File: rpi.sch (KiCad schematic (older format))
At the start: 14 parts, among them J1 40HAT, Q1 DMMT5401, Q2 DMG2305UX, U1 CAT24C32

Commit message: Current snapshot
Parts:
- added H5, H6, H7: 3mm_Mounting_Hole, MountingHole:MountingHole_3mm, symbol Mechanical:MountingHole
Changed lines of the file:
@@
 $Descr A4 11693 8268
 encoding utf-8
-Sheet 2 7
+Sheet 2 11
 Title "Raspberry Pi Connector"
 Date ""
@@
 $EndComp
 NoConn ~ 2650 1900
+$Comp
+L Mechanical:MountingHole H5
+U 1 1 5BC57D78
+P 9050 4600
+F 0 "H5" H 8900 4700 60  0000 C CNN
+F 1 "3mm_Mounting_Hole" H 9050 4450 60  0000 C CNN
+F 2 "MountingHole:MountingHole_3mm" H 8950 4600 60  0001 C CNN
+F 3 "" H 8950 4600 60  0001 C CNN
+	1    9050 4600
+	1    0    0    -1
+$EndComp
+$Comp
+L Mechanical:MountingHole H7
+U 1 1 5BC57D7F
+P 10000 4600
+F 0 "H7" H 9850 4700 60  0000 C CNN
+F 1 "3mm_Mounting_Hole" H 10000 4450 60  0000 C CNN
+F 2 "MountingHole:MountingHole_3mm" H 9900 4600 60  0001 C CNN
+F 3 "" H 9900 4600 60  0001 C CNN
+	1    10000 4600
+	1    0    0    -1
+$EndComp
+$Comp
+L Mechanical:MountingHole H6
+U 1 1 5BC57D86
+P 9050 5100
+F 0 "H6" H 8900 5200 60  0000 C CNN
+F 1 "3mm_Mounting_Hole" H 9050 4950 60  0000 C CNN
+F 2 "MountingHole:MountingHole_3mm" H 8950 5100 60  0001 C CNN
+F 3 "" H 8950 5100 60  0001 C CNN
+	1    9050 5100
+	1    0    0    -1
+$EndComp
 $EndSCHEMATC

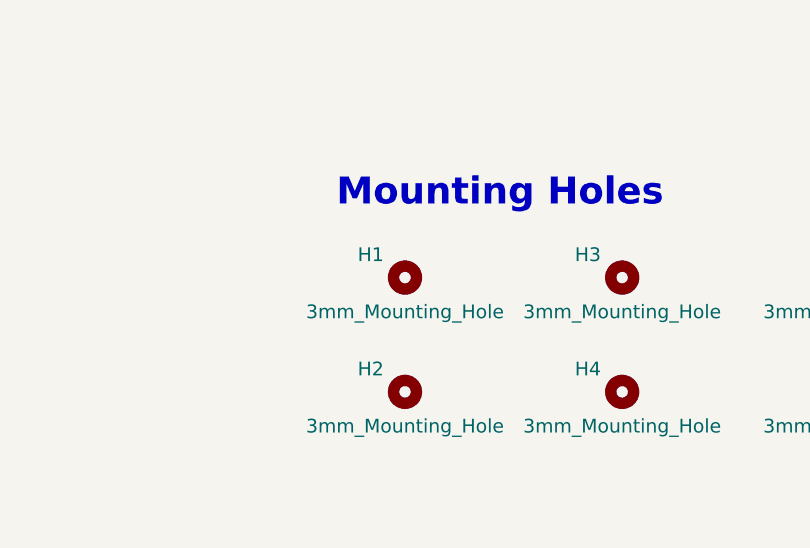
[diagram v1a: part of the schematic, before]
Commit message: Finished general layout and power planes
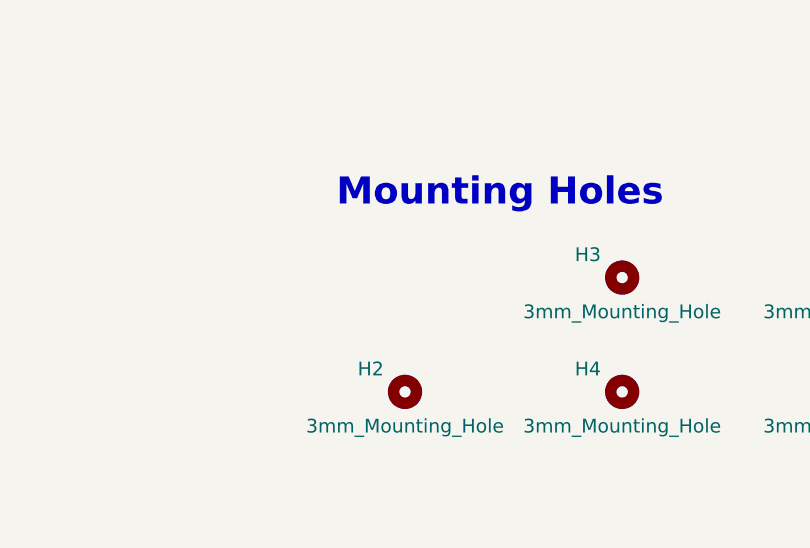
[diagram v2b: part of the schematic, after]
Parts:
- removed H1: 3mm_Mounting_Hole, MountingHole:MountingHole_3mm, symbol Mechanical:MountingHole
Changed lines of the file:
@@
 $EndDescr
-$Comp
-L Mechanical:MountingHole H1
-U 1 1 5BC4B184
-P 7050 4600
-F 0 "H1" H 6900 4700 60  0000 C CNN
-F 1 "3mm_Mounting_Hole" H 7050 4450 60  0000 C CNN
-F 2 "MountingHole:MountingHole_3mm" H 6950 4600 60  0001 C CNN
-F 3 "" H 6950 4600 60  0001 C CNN
-	1    7050 4600
-	1    0    0    -1
-$EndComp
 $Comp
 L heteromycin:OX40HAT J1

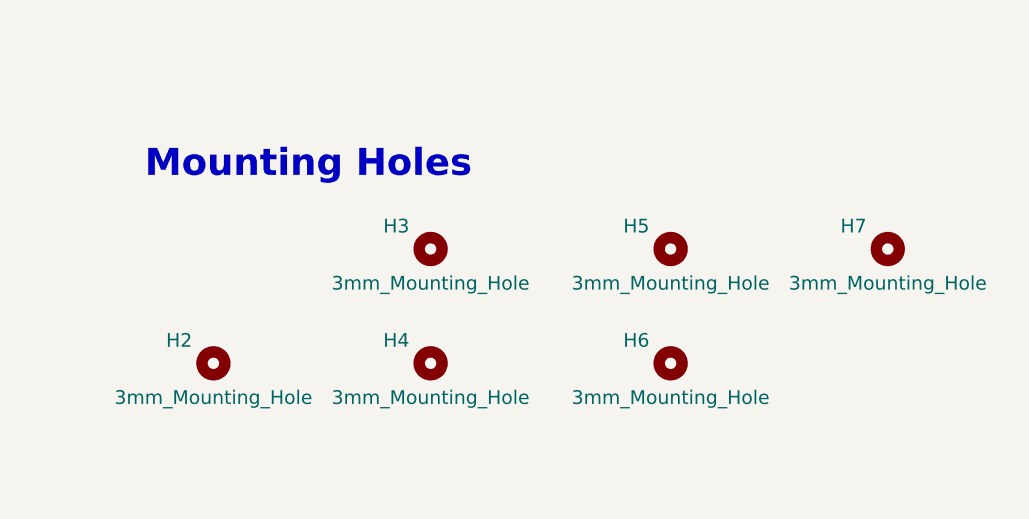
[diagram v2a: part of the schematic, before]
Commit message: Add SD card reader, placed temp connections, fixed stepper placement
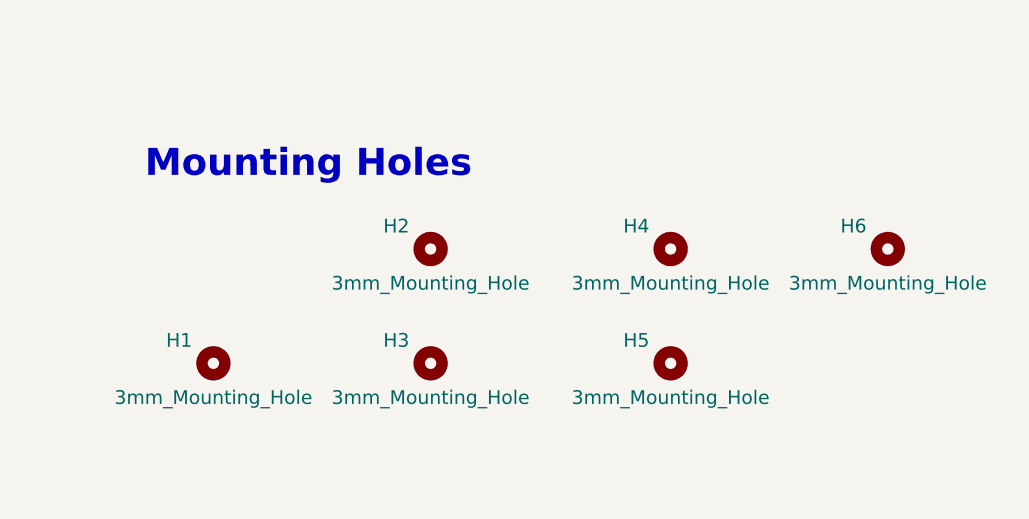
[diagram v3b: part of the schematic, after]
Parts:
- renumbered H2 to H1, H3 to H2, H4 to H3, H5 to H4, H6 to H5, H7 to H6
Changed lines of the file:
@@
 $Descr A4 11693 8268
 encoding utf-8
-Sheet 2 11
+Sheet 2 12
 Title "Raspberry Pi Connector"
 Date ""
@@
 $EndComp
 $Comp
-L Mechanical:MountingHole H3
+L Mechanical:MountingHole H2
 U 1 1 5BC4B22D
 P 8000 4600
-F 0 "H3" H 7850 4700 60  0000 C CNN
+F 0 "H2" H 7850 4700 60  0000 C CNN
 F 1 "3mm_Mounting_Hole" H 8000 4450 60  0000 C CNN
 F 2 "MountingHole:MountingHole_3mm" H 7900 4600 60  0001 C CNN
@@
 $EndComp
 $Comp
-L Mechanical:MountingHole H2
+L Mechanical:MountingHole H1
 U 1 1 5BC4B234
 P 7050 5100
-F 0 "H2" H 6900 5200 60  0000 C CNN
+F 0 "H1" H 6900 5200 60  0000 C CNN
 F 1 "3mm_Mounting_Hole" H 7050 4950 60  0000 C CNN
 F 2 "MountingHole:MountingHole_3mm" H 6950 5100 60  0001 C CNN
@@
 $EndComp
 $Comp
-L Mechanical:MountingHole H4
+L Mechanical:MountingHole H3
 U 1 1 5BC4B23B
 P 8000 5100
-F 0 "H4" H 7850 5200 60  0000 C CNN
+F 0 "H3" H 7850 5200 60  0000 C CNN
 F 1 "3mm_Mounting_Hole" H 8000 4950 60  0000 C CNN
 F 2 "MountingHole:MountingHole_3mm" H 7900 5100 60  0001 C CNN
@@
 NoConn ~ 2650 1900
 $Comp
-L Mechanical:MountingHole H5
+L Mechanical:MountingHole H4
 U 1 1 5BC57D78
 P 9050 4600
-F 0 "H5" H 8900 4700 60  0000 C CNN
+F 0 "H4" H 8900 4700 60  0000 C CNN
 F 1 "3mm_Mounting_Hole" H 9050 4450 60  0000 C CNN
 F 2 "MountingHole:MountingHole_3mm" H 8950 4600 60  0001 C CNN
@@
 $EndComp
 $Comp
-L Mechanical:MountingHole H7
+L Mechanical:MountingHole H6
 U 1 1 5BC57D7F
 P 10000 4600
-F 0 "H7" H 9850 4700 60  0000 C CNN
+F 0 "H6" H 9850 4700 60  0000 C CNN
 F 1 "3mm_Mounting_Hole" H 10000 4450 60  0000 C CNN
 F 2 "MountingHole:MountingHole_3mm" H 9900 4600 60  0001 C CNN
@@
 $EndComp
 $Comp
-L Mechanical:MountingHole H6
+L Mechanical:MountingHole H5
 U 1 1 5BC57D86
 P 9050 5100
-F 0 "H6" H 8900 5200 60  0000 C CNN
+F 0 "H5" H 8900 5200 60  0000 C CNN
 F 1 "3mm_Mounting_Hole" H 9050 4950 60  0000 C CNN
 F 2 "MountingHole:MountingHole_3mm" H 8950 5100 60  0001 C CNN

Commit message: Some small adjustments
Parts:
- J1: value 40HAT -> 920-0135-01
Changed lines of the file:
@@
 P 3250 1100
 F 0 "J1" H 3600 1200 50  0000 C CNN
-F 1 "40HAT" H 2950 1200 50  0000 C CNN
+F 1 "920-0135-01" H 2950 1200 50  0000 C CNN
 F 2 "Connector_PinSocket_2.54mm:PinSocket_2x20_P2.54mm_Vertical" H 3250 1300 50  0001 C CNN
 F 3 "" H 2550 1100 50  0000 C CNN

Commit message: First pass of routing
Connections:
- net RX: now reaches J1.10 (BCM15)
- net nRESET: now reaches J1.12 (BCM18)
- net MOSI: now reaches J1.19 (BCM10)
- net MISO: now reaches J1.21 (BCM9)
- net SCLK: now reaches J1.23 (BCM11)
- net SS_0: now reaches J1.24 (BCM8)
- net SS_1: now reaches J1.26 (BCM7)
- net D1: now reaches J1.29 (BCM5)
- net SDA: now reaches J1.3 (BCM2)
- net D2: now reaches J1.31 (BCM6)
- net D3: now reaches J1.33 (BCM13)
- net D4: now reaches J1.35 (BCM19)
- net SCL: now reaches J1.5 (BCM3)
- net BOOT: now reaches J1.7 (BCM4)
- net TX: now reaches J1.8 (BCM14)
- no-connect marks 2 -> 13
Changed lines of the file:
@@
 	1    0    0    -1
 $EndComp
+Text HLabel 2650 1200 0    50   Input ~ 0
+SDA
+Text HLabel 2650 1300 0    50   Input ~ 0
+SCL
+Text HLabel 2650 1400 0    50   Input ~ 0
+BOOT
+Text HLabel 3850 1600 2    50   Input ~ 0
+nRESET
+Text HLabel 3850 1400 2    50   Input ~ 0
+TX
+Text HLabel 3850 1500 2    50   Input ~ 0
+RX
+Text HLabel 2650 2000 0    50   Input ~ 0
+MOSI
+Text HLabel 2650 2100 0    50   Input ~ 0
+MISO
+Text HLabel 2650 2200 0    50   Input ~ 0
+SCLK
+Text HLabel 3850 2200 2    50   Input ~ 0
+SS_0
+Text HLabel 3850 2300 2    50   Input ~ 0
+SS_1
+Text HLabel 2650 2500 0    50   Input ~ 0
+D1
+Text HLabel 2650 2600 0    50   Input ~ 0
+D2
+Text HLabel 2650 2700 0    50   Input ~ 0
+D3
+Text HLabel 2650 2800 0    50   Input ~ 0
+D4
+NoConn ~ 2650 1600
+NoConn ~ 2650 1700
+NoConn ~ 2650 1800
+NoConn ~ 2650 2900
+NoConn ~ 3850 1800
+NoConn ~ 3850 1900
+NoConn ~ 3850 2100
+NoConn ~ 3850 2600
+NoConn ~ 3850 2800
+NoConn ~ 3850 2900
+NoConn ~ 3850 3000
 $EndSCHEMATC

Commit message: Complete functional design
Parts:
- H1: renamed from H2; footprint MountingHole:MountingHole_3mm -> heteromycin:MountingHole_3mm
- H2: renamed from H1; footprint MountingHole:MountingHole_3mm -> heteromycin:MountingHole_3mm
- H3: renamed from H4; footprint MountingHole:MountingHole_3mm -> heteromycin:MountingHole_3mm
- H4: renamed from H3; footprint MountingHole:MountingHole_3mm -> heteromycin:MountingHole_3mm
- H5: renamed from H6; footprint MountingHole:MountingHole_3mm -> heteromycin:MountingHole_3mm
- H6: renamed from H5; footprint MountingHole:MountingHole_3mm -> heteromycin:MountingHole_3mm
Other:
- moved on the sheet: H1, H3, H4, H5
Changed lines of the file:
@@
+$EndComp
+$Comp
+L Mechanical:MountingHole H1
+U 1 1 5BC4B22D
+P 7050 4600
+F 0 "H1" H 6900 4700 60  0000 C CNN
+F 1 "3mm_Mounting_Hole" H 7050 4450 60  0000 C CNN
+F 2 "heteromycin:MountingHole_3mm" H 6950 4600 60  0001 C CNN
+F 3 "" H 6950 4600 60  0001 C CNN
+	1    7050 4600
+	1    0    0    -1
 $EndComp
 $Comp
 L Mechanical:MountingHole H2
-U 1 1 5BC4B22D
-P 8000 4600
-F 0 "H2" H 7850 4700 60  0000 C CNN
-F 1 "3mm_Mounting_Hole" H 8000 4450 60  0000 C CNN
-F 2 "MountingHole:MountingHole_3mm" H 7900 4600 60  0001 C CNN
-F 3 "" H 7900 4600 60  0001 C CNN
-	1    8000 4600
-	1    0    0    -1
-$EndComp
-$Comp
-L Mechanical:MountingHole H1
 U 1 1 5BC4B234
 P 7050 5100
-F 0 "H1" H 6900 5200 60  0000 C CNN
+F 0 "H2" H 6900 5200 60  0000 C CNN
 F 1 "3mm_Mounting_Hole" H 7050 4950 60  0000 C CNN
-F 2 "MountingHole:MountingHole_3mm" H 6950 5100 60  0001 C CNN
+F 2 "heteromycin:MountingHole_3mm" H 6950 5100 60  0001 C CNN
 F 3 "" H 6950 5100 60  0001 C CNN
 	1    7050 5100
@@
 $EndComp
 $Comp
-L Mechanical:MountingHole H3
+L Mechanical:MountingHole H4
 U 1 1 5BC4B23B
-P 8000 5100
-F 0 "H3" H 7850 5200 60  0000 C CNN
-F 1 "3mm_Mounting_Hole" H 8000 4950 60  0000 C CNN
-F 2 "MountingHole:MountingHole_3mm" H 7900 5100 60  0001 C CNN
-F 3 "" H 7900 5100 60  0001 C CNN
-	1    8000 5100
+P 8050 5100
+F 0 "H4" H 7900 5200 60  0000 C CNN
+F 1 "3mm_Mounting_Hole" H 8050 4950 60  0000 C CNN
+F 2 "heteromycin:MountingHole_3mm" H 7950 5100 60  0001 C CNN
+F 3 "" H 7950 5100 60  0001 C CNN
+	1    8050 5100
 	1    0    0    -1
 $EndComp
@@
 NoConn ~ 2650 1900
 $Comp
-L Mechanical:MountingHole H4
+L Mechanical:MountingHole H3
 U 1 1 5BC57D78
+P 8050 4600
+F 0 "H3" H 7900 4700 60  0000 C CNN
+F 1 "3mm_Mounting_Hole" H 8050 4450 60  0000 C CNN
+F 2 "heteromycin:MountingHole_3mm" H 7950 4600 60  0001 C CNN
+F 3 "" H 7950 4600 60  0001 C CNN
+	1    8050 4600
+	1    0    0    -1
+$EndComp
+$Comp
+L Mechanical:MountingHole H5
+U 1 1 5BC57D7F
 P 9050 4600
-F 0 "H4" H 8900 4700 60  0000 C CNN
+F 0 "H5" H 8900 4700 60  0000 C CNN
 F 1 "3mm_Mounting_Hole" H 9050 4450 60  0000 C CNN
-F 2 "MountingHole:MountingHole_3mm" H 8950 4600 60  0001 C CNN
+F 2 "heteromycin:MountingHole_3mm" H 8950 4600 60  0001 C CNN
 F 3 "" H 8950 4600 60  0001 C CNN
 	1    9050 4600
@@
 $Comp
 L Mechanical:MountingHole H6
-U 1 1 5BC57D7F
-P 10000 4600
-F 0 "H6" H 9850 4700 60  0000 C CNN
-F 1 "3mm_Mounting_Hole" H 10000 4450 60  0000 C CNN
-F 2 "MountingHole:MountingHole_3mm" H 9900 4600 60  0001 C CNN
-F 3 "" H 9900 4600 60  0001 C CNN
-	1    10000 4600
-	1    0    0    -1
-$EndComp
-$Comp
-L Mechanical:MountingHole H5
 U 1 1 5BC57D86
 P 9050 5100
-F 0 "H5" H 8900 5200 60  0000 C CNN
+F 0 "H6" H 8900 5200 60  0000 C CNN
 F 1 "3mm_Mounting_Hole" H 9050 4950 60  0000 C CNN
-F 2 "MountingHole:MountingHole_3mm" H 8950 5100 60  0001 C CNN
+F 2 "heteromycin:MountingHole_3mm" H 8950 5100 60  0001 C CNN
 F 3 "" H 8950 5100 60  0001 C CNN
 	1    9050 5100

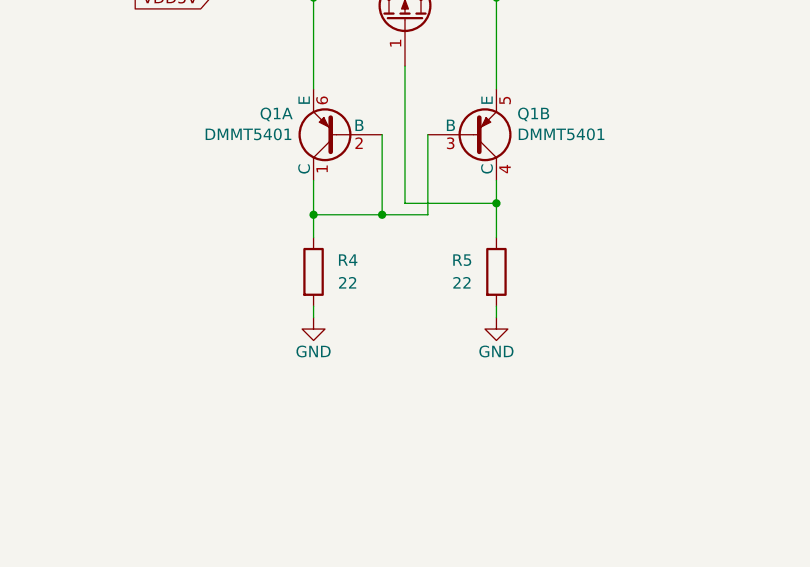
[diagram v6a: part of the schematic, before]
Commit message: Fix ZVD for RPi protection
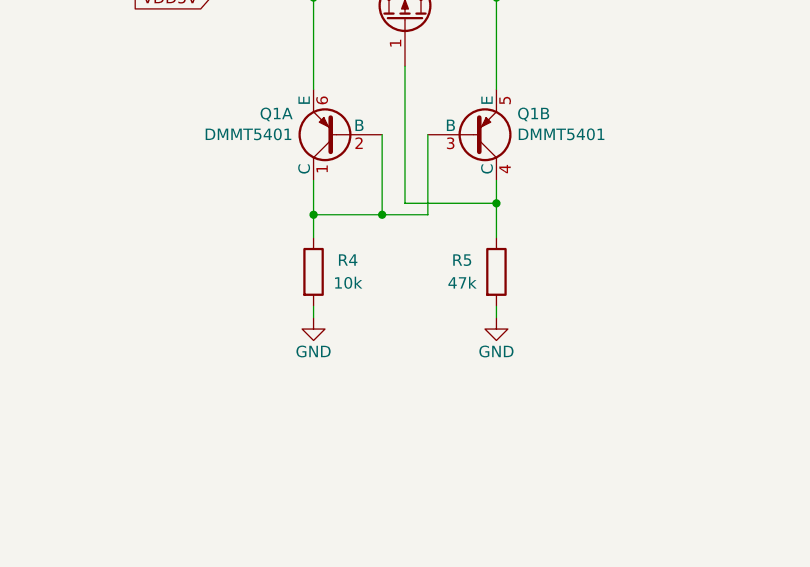
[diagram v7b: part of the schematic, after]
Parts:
- R4: value 22 -> 10k
- R5: value 22 -> 47k
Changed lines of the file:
@@
 P 8200 2450
 F 0 "R5" H 8050 2500 50  0000 C CNN
-F 1 "22" H 8050 2400 50  0000 C CNN
+F 1 "47k" H 8050 2400 50  0000 C CNN
 F 2 "Resistor_SMD:R_0603_1608Metric" V 8130 2450 50  0001 C CNN
 F 3 "" H 8200 2450 50  0001 C CNN
@@
 P 7400 2450
 F 0 "R4" H 7550 2500 50  0000 C CNN
-F 1 "22" H 7550 2400 50  0000 C CNN
+F 1 "10k" H 7550 2400 50  0000 C CNN
 F 2 "Resistor_SMD:R_0603_1608Metric" V 7330 2450 50  0001 C CNN
 F 3 "" H 7400 2450 50  0001 C CNN

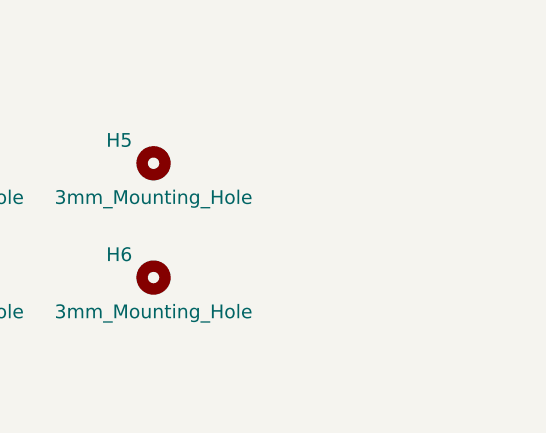
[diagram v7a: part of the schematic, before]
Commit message: Add drawings and another mounting hole
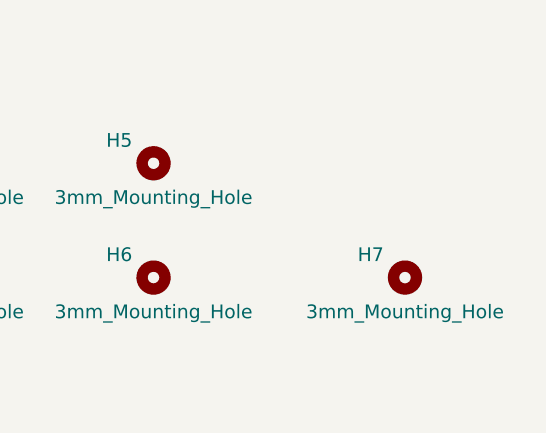
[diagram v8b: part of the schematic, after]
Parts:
- added H7: 3mm_Mounting_Hole, heteromycin:MountingHole_3mm, symbol Mechanical:MountingHole
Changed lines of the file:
@@
 NoConn ~ 3850 2900
 NoConn ~ 3850 3000
+$Comp
+L Mechanical:MountingHole H7
+U 1 1 5BCFB1ED
+P 10150 5100
+F 0 "H7" H 10000 5200 60  0000 C CNN
+F 1 "3mm_Mounting_Hole" H 10150 4950 60  0000 C CNN
+F 2 "heteromycin:MountingHole_3mm" H 10050 5100 60  0001 C CNN
+F 3 "" H 10050 5100 60  0001 C CNN
+	1    10150 5100
+	1    0    0    -1
+$EndComp
 $EndSCHEMATC
